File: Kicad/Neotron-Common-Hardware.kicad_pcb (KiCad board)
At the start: 4 copper layers, 243.8 x 243.8 mm, 161 parts, among them J201 DE15HD, J301 RJ45_Amphenol_RJMG1BD3B8K1ANR, J401 CD Audio In, J402 AC'97 Audio Header, J403 Line Out, J501 USB Ports External, J502 USB Ports Internal, J601 USB_B, J701 Double-mini-DIN-6, J801 Conn_02x05, J802 DB9_Male_MountingHoles, J901 DB9_Female_MountingHoles, U201 TPF133A, U202 TPD7S019, U301 ENC424J600-PT, U401 TLV320AIC23BPW, U402 STX-4335-5BGP-S1, U501 MIC2005A-2YM5, U502 MIC2005A-2YM5, U503 XR22404CG28, U504 MIC2005A-2YM5, U505 MIC2005A-2YM5, U801 ST3232CDR, Y301 25M, Y401 12M, Y501 12M

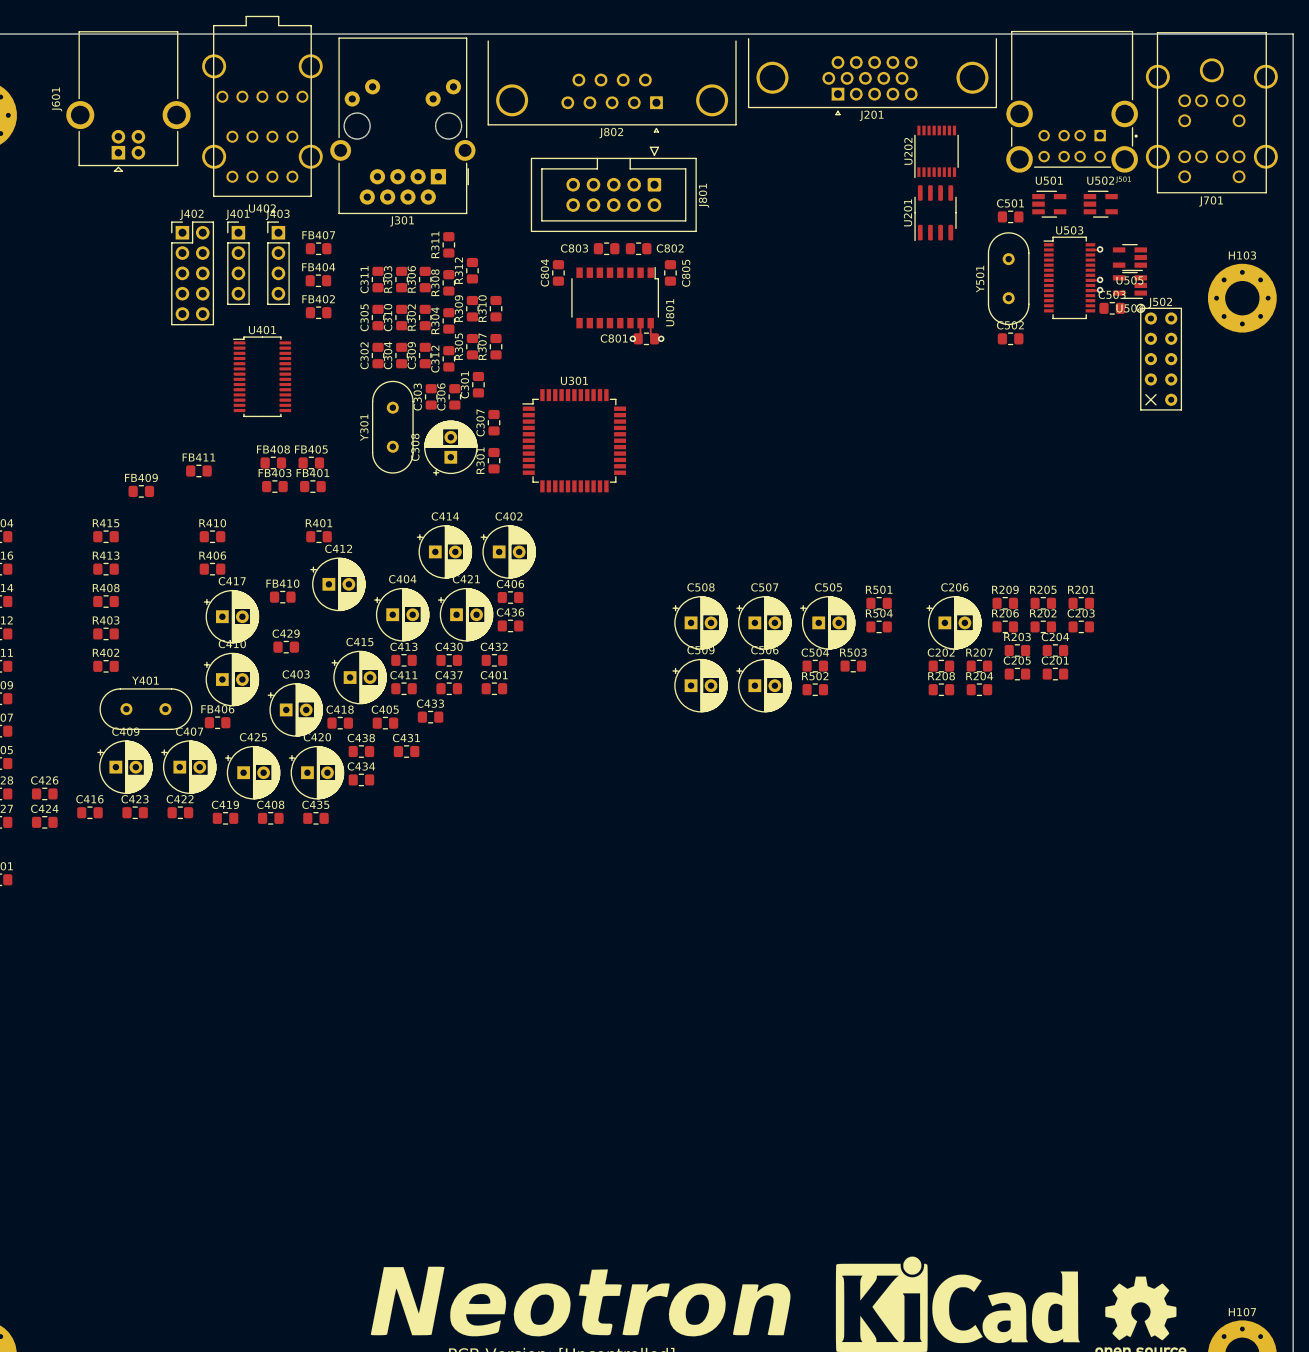
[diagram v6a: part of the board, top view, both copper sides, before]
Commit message: Completed PSU design.
Also changed footprint for stacked USB connector to change
shield pins from SHx to Pin 9.
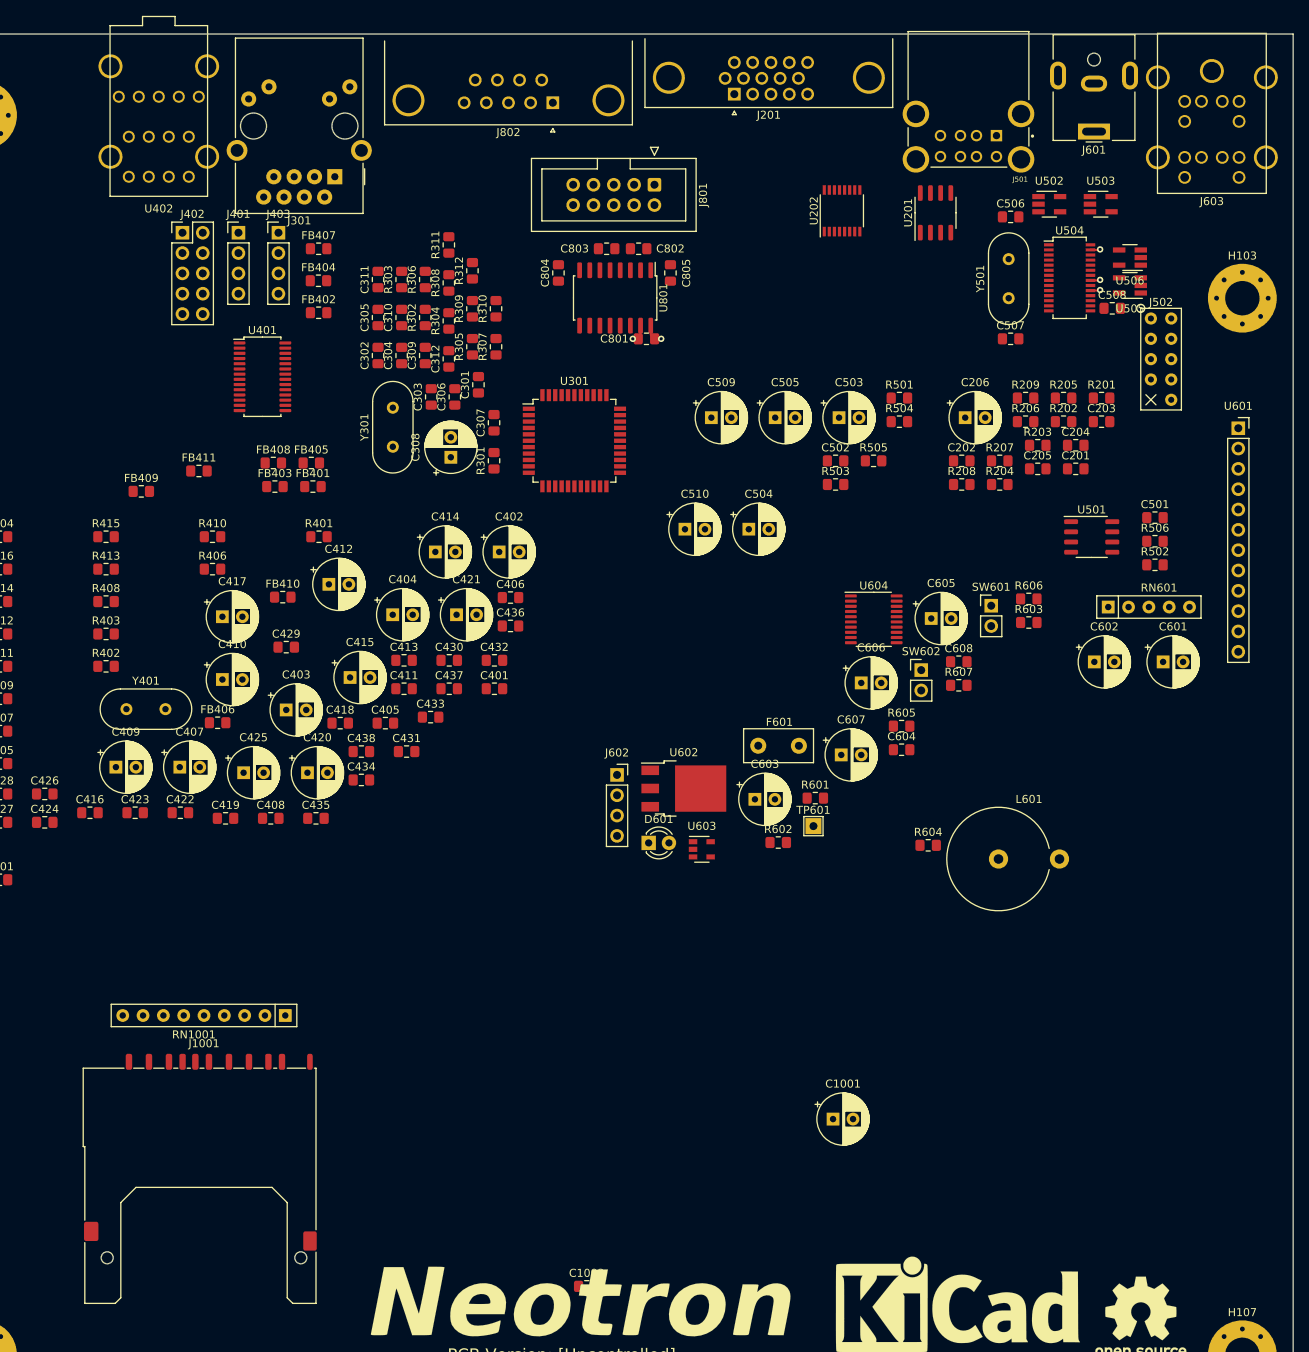
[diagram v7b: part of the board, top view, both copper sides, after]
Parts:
- removed J701: Double-mini-DIN-6, Neotron-Common-Hardware:Double_mini-DIN_6
- added C1001: 10u, Capacitor_THT:CP_Radial_D6.3mm_P2.50mm, F.Cu at (220.1, 166.8)
- added C1002: 100n, Capacitor_SMD:C_0805_2012Metric_Pad1.15x1.40mm_HandSolder, F.Cu at (189.3, 187.7)
- added C501: 100n, Capacitor_SMD:C_0805_2012Metric_Pad1.15x1.40mm_HandSolder, F.Cu at (260.3, 91.6)
- added C601: 100u, Capacitor_THT:CP_Radial_D6.3mm_P2.50mm, F.Cu at (261.3, 109.7)
- added C602: 100u, Capacitor_THT:CP_Radial_D6.3mm_P2.50mm, F.Cu at (252.7, 109.7)
- added C603: 22u, Capacitor_THT:CP_Radial_D6.3mm_P2.50mm, F.Cu at (210.3, 126.8)
- added C604: 100n, Capacitor_SMD:C_0805_2012Metric_Pad1.15x1.40mm_HandSolder, F.Cu at (228.7, 120.6)
- added C605: 47u, Capacitor_THT:CP_Radial_D6.3mm_P2.50mm, F.Cu at (232.4, 104.2)
- added C606: 1u, Capacitor_THT:CP_Radial_D6.3mm_P2.50mm, F.Cu at (223.6, 112.3)
- added C607: 4u7, Capacitor_THT:CP_Radial_D6.3mm_P2.50mm, F.Cu at (221.1, 121.3)
- added C608: 100n, Capacitor_SMD:C_0805_2012Metric_Pad1.15x1.40mm_HandSolder, F.Cu at (235.8, 109.6)
- added D601: LED, LED_THT:LED_D3.0mm, F.Cu at (197.0, 132.3)
- added F601: 5A Polyfuse, Fuse:Fuse_Littelfuse_395Series, F.Cu at (210.7, 120.1)
- added J1001: SD_Card, Connector_Card:SD_Kyocera_145638109511859+, F.Cu at (141.5, 172.2)
- added J602: Conn_01x04, Connector_PinSocket_2.54mm:PinSocket_1x04_P2.54mm_Vertical, F.Cu at (193.1, 123.8)
- added J603: Double-mini-DIN-6, Neotron-Common-Hardware:Double_mini-DIN_6, F.Cu at (267.4, 42.1)
- added L601: 22u, Inductor_THT:L_Axial_L23.4mm_D12.7mm_P7.62mm_Vertical_Vishay_IHA-203, F.Cu at (240.8, 134.3)
- added R502: 10k, Resistor_SMD:R_0805_2012Metric_Pad1.15x1.40mm_HandSolder, F.Cu at (260.3, 97.5)
- added R506: 10k, Resistor_SMD:R_0805_2012Metric_Pad1.15x1.40mm_HandSolder, F.Cu at (260.3, 94.6)
- added R601: 100k, Resistor_SMD:R_0805_2012Metric_Pad1.15x1.40mm_HandSolder, F.Cu at (217.9, 126.7)
- added R602: 100k, Resistor_SMD:R_0805_2012Metric_Pad1.15x1.40mm_HandSolder, F.Cu at (213.2, 132.2)
- added R603: 100k, Resistor_SMD:R_0805_2012Metric_Pad1.15x1.40mm_HandSolder, F.Cu at (244.6, 104.7)
- added R604: 100k, Resistor_SMD:R_0805_2012Metric_Pad1.15x1.40mm_HandSolder, F.Cu at (232.0, 132.6)
- added R605: 100k, Resistor_SMD:R_0805_2012Metric_Pad1.15x1.40mm_HandSolder, F.Cu at (228.7, 117.7)
- added R606: 100k, Resistor_SMD:R_0805_2012Metric_Pad1.15x1.40mm_HandSolder, F.Cu at (244.6, 101.8)
- added R607: 1k, Resistor_SMD:R_0805_2012Metric_Pad1.15x1.40mm_HandSolder, F.Cu at (235.8, 112.6)
- added RN1001: 8x10k, Resistor_THT:R_Array_SIP9, F.Cu at (151.6, 153.9)
- added RN601: 2k7 x 4, Resistor_THT:R_Array_SIP5, F.Cu at (254.5, 102.8)
- added SW601: SW_DIP_x01, Connector_PinHeader_2.54mm:PinHeader_1x02_P2.54mm_Vertical, F.Cu at (239.9, 102.6)
- added SW602: SW_DIP_x01, Connector_PinHeader_2.54mm:PinHeader_1x02_P2.54mm_Vertical, F.Cu at (231.1, 110.7)
- added TP601: TestPoint, TestPoint:TestPoint_THTPad_2.0x2.0mm_Drill1.0mm, F.Cu at (217.6, 130.2)
- added U501: AP2501, Package_SO:SO-8_3.9x4.9mm_P1.27mm, F.Cu at (252.4, 94.0)
- added U601: K7805-3AR3, Connector_PinSocket_2.54mm:PinSocket_1x12_P2.54mm_Vertical, F.Cu at (270.7, 80.5)
- added U602: AMS1117CD-3.3, Package_TO_SOT_SMD:TO-252-3_TabPin2, F.Cu at (201.4, 125.5)
- added U603: MAX1615xUK, Package_TO_SOT_SMD:SOT-23-5, F.Cu at (203.7, 133.1)
- added U604: NUC029FAE, Package_SO:TSSOP-20_4.4x6.5mm_P0.65mm, F.Cu at (225.2, 104.3)
- J601: value USB_B -> Jack-DC; footprint Connector_USB:USB_B_OST_USB-B1HSxx_Horizontal -> Connector_BarrelJack:BarrelJack_CUI_PJ-063AH_Horizontal
- U801: footprint Package_SO:SOP-16_4.4x10.4mm_P1.27mm -> Package_SO:SO-16_5.3x10.2mm_P1.27mm
- moved J601 122.0 mm to (252.7, 43.4), turned to 180 degrees
- moved C203 25.8 mm to (253.7, 79.6)
- moved C206 25.8 mm to (236.6, 79.1)
- moved C503 25.8 mm to (220.8, 79.1)
- moved C505 25.8 mm to (212.9, 79.1)
- moved C509 25.8 mm to (204.9, 79.1)
- moved R202 25.8 mm to (248.9, 79.6)
- moved R206 25.8 mm to (244.2, 79.6)
- moved R504 25.8 mm to (228.4, 79.6)
- moved C201 25.8 mm to (250.4, 85.5)
- moved C202 25.8 mm to (236.2, 84.5)
- moved C204 25.8 mm to (250.4, 82.6)
- moved C205 25.8 mm to (245.7, 85.5)
- moved C502 25.8 mm to (220.4, 84.5)
- moved R201 25.8 mm to (253.7, 76.7)
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- renumbered C504 to C502, C505 to C503, C506 to C504, C507 to C505, C501 to C506, C502 to C507, C503 to C508, C508 to C509, C509 to C510, R502 to R503, R503 to R505, U501 to U502, U502 to U503, U503 to U504, U504 to U505, U505 to U506
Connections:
- C502 pad 1: +3V3 -> /USB/USB_5V
- C503 pad 1: +3V3 -> /USB/USB_5V
- C805 pad 1: +3V3 -> GND
- J601 pad 1: (no net) -> Net-(F601-Pad2)
- J601 pad 2: (no net) -> GND
- R504 pad 1: +5V -> /USB/USB_5V
- U502 pad 1: +5V -> /USB/USB_5V
- U503 pad 1: +5V -> /USB/USB_5V
- U504 pad 20: (no net) -> /USB/USB_5V
- U504 pad 21: +3V3 -> (no net)
- U504 pad 22: GND -> Net-(R506-Pad1)
- U505 pad 1: +5V -> /USB/USB_5V
- U506 pad 1: +5V -> /USB/USB_5V
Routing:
- net (no net): track 0.00 -> 1.24 mm, vias 0 -> 1
- net +3V3: track 5.98 -> 4.74 mm, vias 4 -> 3

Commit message: Replaced NUC029 (TSSOP) with KE04 (SOIC).
Also updated the BOM with some part nos.
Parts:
- added R605: 33k, Resistor_SMD:R_0805_2012Metric_Pad1.15x1.40mm_HandSolder, F.Cu at (183.1, 147.9)
- R604: value 100k -> 1k
- R607: value 1k -> 100k
- TP601: value TestPoint -> Reset
- U604: value NUC029FAE -> MKE04P24M48SF0; footprint Package_SO:TSSOP-20_4.4x6.5mm_P0.65mm -> Package_SO:SOIC-20W_7.5x12.8mm_P1.27mm
- moved R603 73.5 mm to (183.1, 144.9)
- moved U604 68.9 mm to (169.6, 145.1)
- moved R607 65.0 mm to (183.2, 150.8)
- moved R604 45.9 mm to (187.8, 144.9)
- moved R602 39.8 mm to (178.4, 151.6)
- moved J602 22.0 mm to (178.4, 140.2)
- moved D601 16.9 mm to (182.3, 140.7)
- renumbered R605 to R606, R606 to R608
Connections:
- J602 pad 1: /Power Supply/ICE_CLK -> /Power Supply/SWDCLK
- J602 pad 2: /Power Supply/ICE_DAT -> /Power Supply/SWDIO
- R602 pad 2: /Power Supply/ICE_CLK -> /Power Supply/SWDCLK
- R603 pad 2: /Power Supply/ICE_DAT -> /Power Supply/SWDIO
- R604 pad 1: +3V3 -> /Power Supply/STATUS_LED
- R604 pad 2: /Power Supply/MONITOR_3V3 -> Net-(D601-Pad2)
- R606 pad 2: /Power Supply/MONITOR_5V -> /Power Supply/MON_5V
- R607 pad 1: /Power Supply/STATUS_LED -> /Power Supply/MON_3V3
- R607 pad 2: Net-(D601-Pad2) -> GND
- R608 pad 1: /Power Supply/MONITOR_5V -> /Power Supply/MON_5V
- U604 pad 1: /Power Supply/MONITOR_3V3 -> Net-(TP601-Pad1)
- U604 pad 10: /Power Supply/~RESET_SW -> /Power Supply/PS2_CLK1
- U604 pad 11: GND -> /Power Supply/PS2_DAT0
- U604 pad 12: /Power Supply/STATUS_LED -> /Power Supply/PS2_CLK0
- U604 pad 13: /Power Supply/DC_ON -> /Power Supply/~RESET_SW
- U604 pad 14: /Power Supply/ICE_CLK -> (no net)
- U604 pad 15: /Power Supply/ICE_DAT -> /Power Supply/UART0_TX
- U604 pad 16: /Power Supply/PS2_DAT1 -> /Power Supply/MON_3V3
- U604 pad 17: /Power Supply/PS2_CLK1 -> (no net)
- U604 pad 18: /Power Supply/PS2_DAT0 -> (no net)
- U604 pad 19: /Power Supply/PS2_CLK0 -> /Power Supply/MON_5V
- U604 pad 2: /Power Supply/UART0_TX -> /Power Supply/SWDIO
- U604 pad 20: +5VP -> /Power Supply/SWDCLK
- U604 pad 3: /Power Supply/MONITOR_5V -> +5VP
- U604 pad 4: (no net) -> GND
- U604 pad 5: Net-(TP601-Pad1) -> /Power Supply/STATUS_LED
- U604 pad 6: (no net) -> /Power Supply/DC_ON
- U604 pad 8: (no net) -> /Power Supply/~POWER_SW
- U604 pad 9: /Power Supply/~POWER_SW -> /Power Supply/PS2_DAT1
